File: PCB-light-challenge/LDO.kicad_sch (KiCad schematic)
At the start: 3 parts

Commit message: Footprint van de eds protection device aangepast naar sod 523
https://nl.farnell.com/en-NL/rohm/rsb6-8smt2n/esd-protection-diode-sod-523-2/dp/2914120
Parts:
- D1: footprint Diode_SMD:D_SOD-323_HandSoldering -> Diode_SMD:D_SOD-523
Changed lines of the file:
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@@
       (effects (font (size 1.27 1.27)) (justify right) hide)
     )
-    (property "Footprint" "Diode_SMD:D_SOD-323_HandSoldering" (at 100.965 68.58 0)
+    (property "Footprint" "Diode_SMD:D_SOD-523" (at 100.965 68.58 0)
       (effects (font (size 1.27 1.27)) hide)
     )

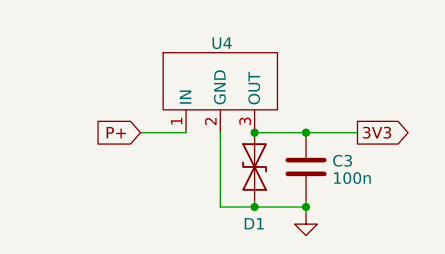
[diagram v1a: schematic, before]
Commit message: TP footprint verandert,  apparte grond (P-) gemaakt.  AC  clearance verandert.  connector voor PIR verandert
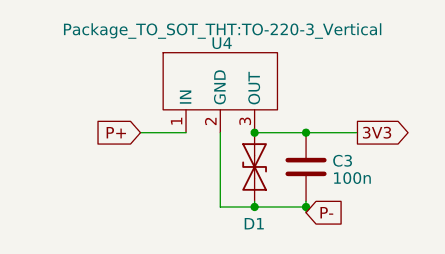
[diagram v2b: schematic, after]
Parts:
- U4: footprint LDO:LDO- TO220FP -> Package_TO_SOT_THT:TO-220-3_Vertical
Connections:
- net GND renamed P-
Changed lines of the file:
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@@
+    )
+  )
+  (global_label "P-" (shape input) (at 106.68 73.66 0) (fields_autoplaced)
+    (effects (font (size 1.27 1.27)) (justify left))
+    (property "Intersheetrefs" "${INTERSHEET_REFS}" (at 112.4282 73.66 0)
+      (effects (font (size 1.27 1.27)) (justify left) hide)
     )
   )
@@
       (effects (font (size 1.27 1.27)) hide)
     )
-    (property "Footprint" "LDO:LDO- TO220FP" (at 97.409 53.34 0)
-      (effects (font (size 1.27 1.27)) hide)
+    (property "Footprint" "Package_TO_SOT_THT:TO-220-3_Vertical" (at 97.409 53.34 0)
+      (effects (font (size 1.27 1.27)))
     )
     (property "Datasheet" "" (at 97.155 57.15 0)
@@
         )
       )
-    )
-  )
-  (symbol (lib_id "power:GND") (at 106.68 73.66 0) (unit 1)
-    (in_bom yes) (on_board yes) (dnp no) (fields_autoplaced)
-    (property "Reference" "#PWR024" (at 106.68 80.01 0)
-      (effects (font (size 1.27 1.27)) hide)
-    )
-    (property "Value" "GND" (at 106.68 77.7955 0)
-      (effects (font (size 1.27 1.27)) hide)
-    )
-    (property "Footprint" "" (at 106.68 73.66 0)
-      (effects (font (size 1.27 1.27)) hide)
-    )
-    (property "Datasheet" "" (at 106.68 73.66 0)
-      (effects (font (size 1.27 1.27)) hide)
-    )
-    (pin "1")
-    (instances
-      (project "PCB-light-challenge"
-        (path "/35573e8f-7834-430c-81d2-239f316c7834/2e4391fc-91c5-40c6-9f1e-d883ea305622"
-          (reference "#PWR024") (unit 1)
-        )
-        (path "/35573e8f-7834-430c-81d2-239f316c7834/a8982b6c-f9f4-4ae9-b882-3fbabc855f32"
-          (reference "#PWR026") (unit 1)
-        )
-      )

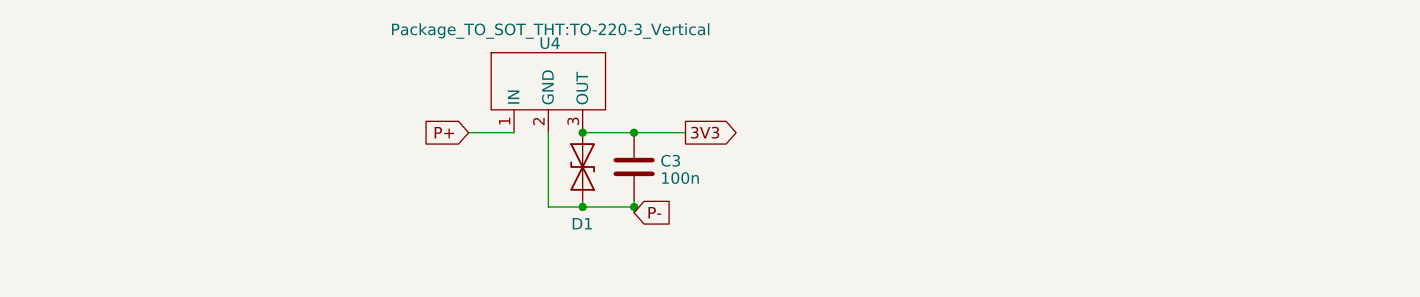
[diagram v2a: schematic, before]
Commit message: Vias  kleiner gemaakt en grond GND genoemd op silkscreen
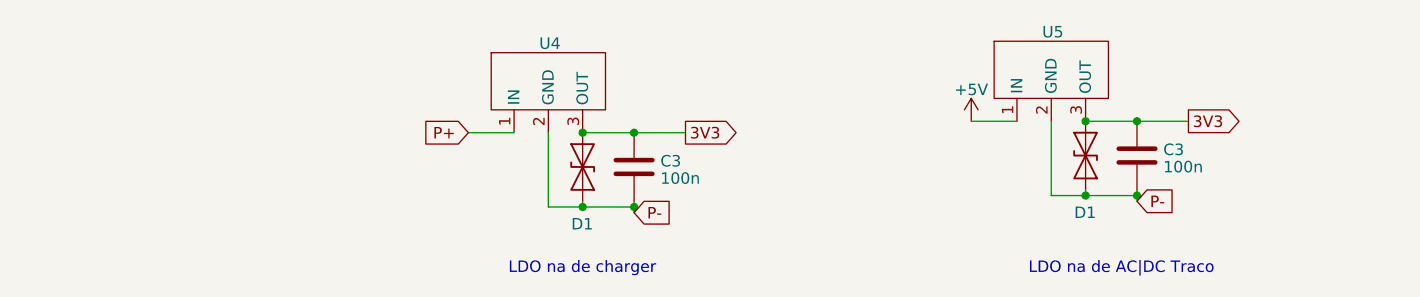
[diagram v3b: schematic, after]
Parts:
- added C3: 100n, Capacitor_SMD:C_0603_1608Metric, symbol Device:C
- added D1: ESD9B3.3ST5G, Diode_SMD:D_SOD-523, symbol Diode:ESD9B3.3ST5G
- added U5: ~, Package_TO_SOT_THT:TO-220-3_Vertical, symbol LDO:BA33DD0T-TO220FP
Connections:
- net 3V3: now also C3.1, D1.2 (A2), U5.3 (OUT)
- net P-: now also C3.2, D1.1 (A1), U5.2 (GND)
- new net +5V: U5.1 (IN)
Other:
- note added: "LDO na de AC|DC Traco"
- note added: "LDO na de charger"
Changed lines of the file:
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@@
   (junction (at 106.68 64.77) (diameter 0) (color 0 0 0 0)
   )
+  (junction (at 162.56 63.5) (diameter 0) (color 0 0 0 0)
+  )
+  (junction (at 162.56 71.755) (diameter 0) (color 0 0 0 0)
+  )
   (junction (at 106.68 73.025) (diameter 0) (color 0 0 0 0)
   )
+  (junction (at 156.845 71.755) (diameter 0) (color 0 0 0 0)
+  )
   (junction (at 100.965 73.025) (diameter 0) (color 0 0 0 0)
   )
+  (junction (at 156.845 63.5) (diameter 0) (color 0 0 0 0)
+  )
   (wire (pts (xy 106.68 73.025) (xy 106.68 73.66))
     (stroke (width 0) (type default))
@@
     (stroke (width 0) (type default))
   )
+  (wire (pts (xy 156.845 63.5) (xy 162.56 63.5))
+    (stroke (width 0) (type default))
+  )
+  (wire (pts (xy 162.56 71.755) (xy 162.56 72.39))
+    (stroke (width 0) (type default))
+  )
   (wire (pts (xy 106.68 64.77) (xy 112.395 64.77))
     (stroke (width 0) (type default))
   )
+  (wire (pts (xy 153.035 63.5) (xy 153.035 71.755))
+    (stroke (width 0) (type default))
+  )
   (wire (pts (xy 106.68 72.39) (xy 106.68 73.025))
     (stroke (width 0) (type default))
@@
     (stroke (width 0) (type default))
   )
+  (wire (pts (xy 144.145 63.5) (xy 149.225 63.5))
+    (stroke (width 0) (type default))
+  )
+  (wire (pts (xy 162.56 63.5) (xy 168.275 63.5))
+    (stroke (width 0) (type default))
+  )
+  (wire (pts (xy 156.845 71.12) (xy 156.845 71.755))
+    (stroke (width 0) (type default))
+  )
   (wire (pts (xy 100.965 72.39) (xy 100.965 73.025))
     (stroke (width 0) (type default))
@@
     (stroke (width 0) (type default))
   )
+  (wire (pts (xy 162.56 71.12) (xy 162.56 71.755))
+    (stroke (width 0) (type default))
+  )
+  (wire (pts (xy 153.035 71.755) (xy 156.845 71.755))
+    (stroke (width 0) (type default))
+  )
+  (wire (pts (xy 156.845 71.755) (xy 162.56 71.755))
+    (stroke (width 0) (type default))
+  )
+  (text "LDO na de AC|DC Traco" (at 150.495 80.645 0)
+    (effects (font (size 1.27 1.27)) (justify left bottom))
+  )
+  (text "LDO na de charger" (at 92.71 80.645 0)
+    (effects (font (size 1.27 1.27)) (justify left bottom))
+  )
   (global_label "3V3" (shape output) (at 112.395 64.77 0) (fields_autoplaced)
     (effects (font (size 1.27 1.27)) (justify left))
@@
     )
   )
-  (global_label "P+" (shape input) (at 88.2904 64.77 180) (fields_autoplaced)
+  (global_label "P-" (shape input) (at 162.56 72.39 0) (fields_autoplaced)
+    (effects (font (size 1.27 1.27)) (justify left))
+    (property "Intersheetrefs" "${INTERSHEET_REFS}" (at 168.3082 72.39 0)
+      (effects (font (size 1.27 1.27)) (justify left) hide)
+    )
+  )
+  (global_label "P+" (shape input) (at 88.265 64.77 180) (fields_autoplaced)
     (effects (font (size 1.27 1.27)) (justify right))
-    (property "Intersheetrefs" "${INTERSHEET_REFS}" (at 82.5422 64.77 0)
+    (property "Intersheetrefs" "${INTERSHEET_REFS}" (at 82.5168 64.77 0)
       (effects (font (size 1.27 1.27)) (justify right) hide)
     )
   )
-  (symbol (lib_id "LDO:BA33DD0T-TO220FP") (at 97.155 57.15 0) (unit 1)
+  (global_label "3V3" (shape output) (at 168.275 63.5 0) (fields_autoplaced)
+    (effects (font (size 1.27 1.27)) (justify left))
+    (property "Intersheetrefs" "${INTERSHEET_REFS}" (at 174.6884 63.5 0)
+      (effects (font (size 1.27 1.27)) (justify left) hide)
+    )
+  )
+  (symbol (lib_name "BA33DD0T-TO220FP_1") (lib_id "LDO:BA33DD0T-TO220FP") (at 97.155 57.15 0) (unit 1)
     (in_bom yes) (on_board yes) (dnp no)
     (property "Reference" "U4" (at 96.139 54.864 0)
@@
     )
     (property "Footprint" "Package_TO_SOT_THT:TO-220-3_Vertical" (at 97.409 53.34 0)
-      (effects (font (size 1.27 1.27)))
+      (effects (font (size 1.27 1.27)) hide)
     )
     (property "Datasheet" "" (at 97.155 57.15 0)
@@
     )
   )
+  (symbol (lib_id "LDO:BA33DD0T-TO220FP") (at 153.035 55.88 0) (unit 1)
+    (in_bom yes) (on_board yes) (dnp no)
+    (property "Reference" "U5" (at 152.019 53.594 0)
+      (effects (font (size 1.27 1.27)) (justify left))
+    )
+    (property "Value" "~" (at 155.575 54.102 0)
+      (effects (font (size 1.27 1.27)) hide)
+    )
+    (property "Footprint" "Package_TO_SOT_THT:TO-220-3_Vertical" (at 153.289 52.07 0)
+      (effects (font (size 1.27 1.27)) hide)
+    )
+    (property "Datasheet" "" (at 153.035 55.88 0)
+      (effects (font (size 1.27 1.27)) hide)
+    )
+    (pin "1")
+    (pin "2")
+    (pin "3")
+    (instances
+      (project "PCB-light-challenge"
+        (path "/35573e8f-7834-430c-81d2-239f316c7834/a8982b6c-f9f4-4ae9-b882-3fbabc855f32"
+          (reference "U5") (unit 1)
+        )
+      )
+    )
+  )
   (symbol (lib_id "Diode:ESD9B3.3ST5G") (at 100.965 68.58 90) (unit 1)
     (in_bom yes) (on_board yes) (dnp no)
@@
         )
       )
+    )
+  )
+  (symbol (lib_id "power:+5V") (at 144.145 63.5 0) (unit 1)
+    (in_bom yes) (on_board yes) (dnp no) (fields_autoplaced)
+    (property "Reference" "#PWR02" (at 144.145 67.31 0)
+      (effects (font (size 1.27 1.27)) hide)
+    )
+    (property "Value" "+5V" (at 144.145 59.9981 0)
+      (effects (font (size 1.27 1.27)))
+    )
+    (property "Footprint" "" (at 144.145 63.5 0)
+      (effects (font (size 1.27 1.27)) hide)
+    )
+    (property "Datasheet" "" (at 144.145 63.5 0)
+      (effects (font (size 1.27 1.27)) hide)
+    )
+    (pin "1")
+    (instances
+      (project "PCB-light-challenge"
+        (path "/35573e8f-7834-430c-81d2-239f316c7834/a8982b6c-f9f4-4ae9-b882-3fbabc855f32"
+          (reference "#PWR02") (unit 1)
+        )
+      )
+    )
+  )
+  (symbol (lib_id "Diode:ESD9B3.3ST5G") (at 156.845 67.31 90) (unit 1)
+    (in_bom yes) (on_board yes) (dnp no)
+    (property "Reference" "D1" (at 155.575 73.66 90)
+      (effects (font (size 1.27 1.27)) (justify right))
+    )
+    (property "Value" "ESD9B3.3ST5G" (at 160.02 68.58 90)
+      (effects (font (size 1.27 1.27)) (justify right) hide)
+    )
+    (property "Footprint" "Diode_SMD:D_SOD-523" (at 156.845 67.31 0)
+      (effects (font (size 1.27 1.27)) hide)
+    )
+    (property "Datasheet" "https://www.onsemi.com/pub/Collateral/ESD9B-D.PDF" (at 156.845 67.31 0)
+      (effects (font (size 1.27 1.27)) hide)
+    )
+    (pin "1")
+    (pin "2")
+    (instances
+      (project "PCB-light-challenge"
+        (path "/35573e8f-7834-430c-81d2-239f316c7834/1ee2b17a-9b36-4608-9d61-b871128bc979"
+          (reference "D1") (unit 1)
+        )
+        (path "/35573e8f-7834-430c-81d2-239f316c7834/a8982b6c-f9f4-4ae9-b882-3fbabc855f32"
+          (reference "D3") (unit 1)
+        )
+      )
+    )
+  )
+  (symbol (lib_id "Device:C") (at 162.56 67.31 0) (unit 1)
+    (in_bom yes) (on_board yes) (dnp no) (fields_autoplaced)
+    (property "Reference" "C3" (at 165.481 66.6663 0)
+      (effects (font (size 1.27 1.27)) (justify left))
+    )
+    (property "Value" "100n" (at 165.481 68.5873 0)
+      (effects (font (size 1.27 1.27)) (justify left))
+    )
+    (property "Footprint" "Capacitor_SMD:C_0603_1608Metric" (at 163.5252 71.12 0)
+      (effects (font (size 1.27 1.27)) hide)
+    )
+    (property "Datasheet" "~" (at 162.56 67.31 0)
+      (effects (font (size 1.27 1.27)) hide)
+    )
+    (pin "1")
+    (pin "2")
+    (instances
+      (project "PCB-light-challenge"
+        (path "/35573e8f-7834-430c-81d2-239f316c7834/2e4391fc-91c5-40c6-9f1e-d883ea305622"
+          (reference "C3") (unit 1)
+        )
+        (path "/35573e8f-7834-430c-81d2-239f316c7834/a8982b6c-f9f4-4ae9-b882-3fbabc855f32"
+          (reference "C3") (unit 1)
+        )
+      )

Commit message: Extra caps
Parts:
- added C10, C4, C6, C8: C_Polarized, Capacitor_THT:CP_Radial_Tantal_D5.5mm_P2.50mm, symbol Device:C_Polarized
- added C3 (x2): 100n, Capacitor_SMD:C_0603_1608Metric, symbol Device:C
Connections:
- net +5V: now also C10.1, C3.1
- net 3V3: now also C4.1, C6.1
- net P+: now also C3.1, C8.1
- net P-: now also C10.2, C3.2, C3.2, C4.2, C6.2, C8.2
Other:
- moved on the sheet: C3, D1, U4
